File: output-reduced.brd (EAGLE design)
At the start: 31.8 x 81.7 mm, 84 parts

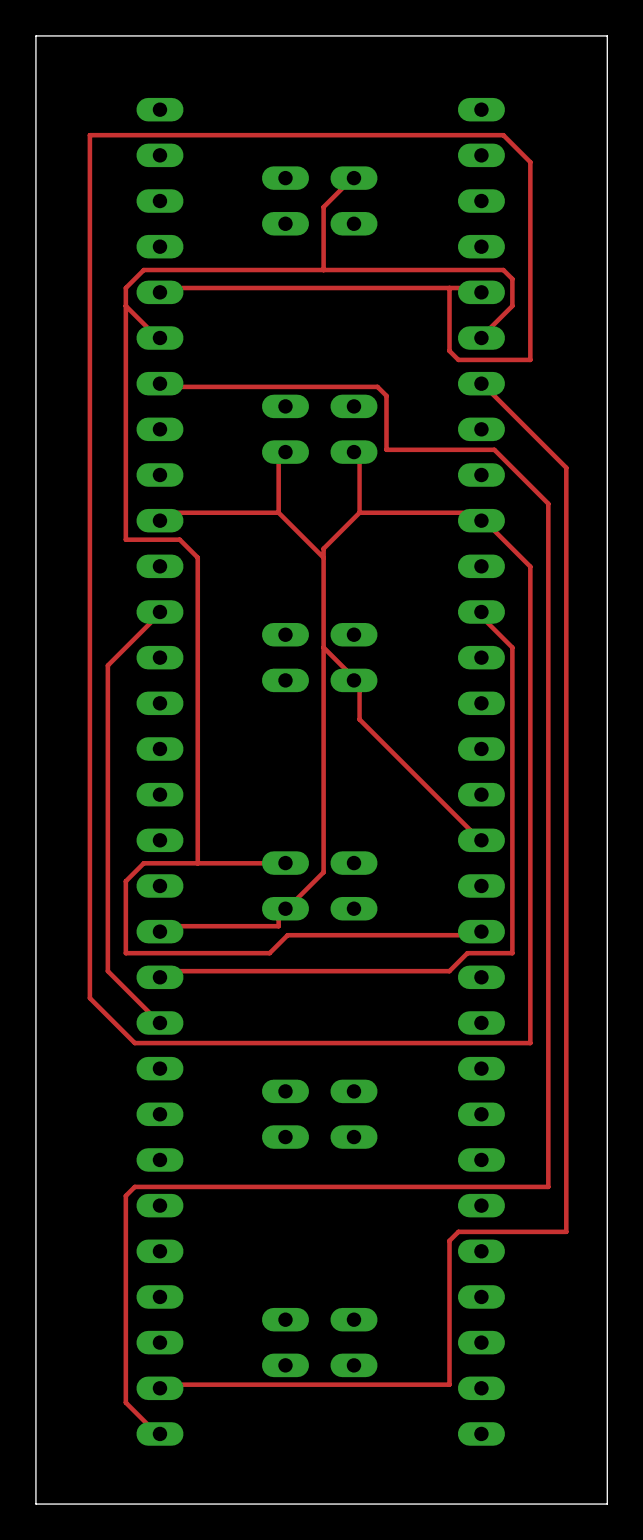
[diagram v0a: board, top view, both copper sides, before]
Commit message: new CirclingCar circuit
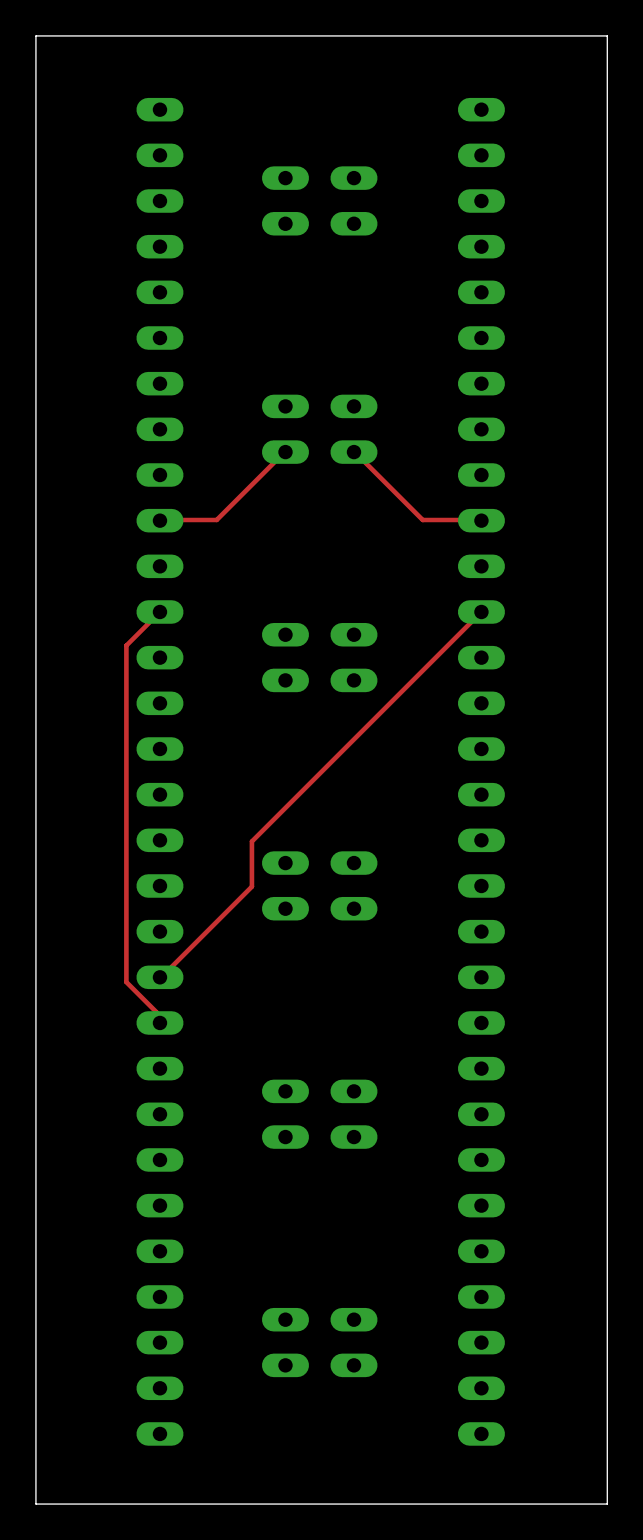
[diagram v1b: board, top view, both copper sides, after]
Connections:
- removed net SIGNAL4: LL5.P$1, LS6.P$1, RL18.P$1, RL5.P$1, RS0.P$1
- removed net SIGNAL5: LL18.P$1, LL4.P$1, LL9.P$1, LS3.P$1, LS7.P$1, RL16.P$1, RL4.P$1, RL9.P$1, RS3.P$1, RS5.P$1
- net SIGNAL0: now also LL19.P$1, RL11.P$1; no longer LL28.P$1, RL6.P$1
- net SIGNAL1: now also LL11.P$1, LL20.P$1; no longer LL29.P$1, LL6.P$1
- net SIGNAL2: now also LL9.P$1, LS3.P$1; no longer LL19.P$1, RL11.P$1
- net SIGNAL3: now also RL9.P$1, RS3.P$1; no longer LL11.P$1, LL20.P$1
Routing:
- net SIGNAL5: track 237.1 -> 0.00 mm
- net SIGNAL4: track 103.5 -> 0.00 mm
- net SIGNAL1: track 101.9 -> 24.5 mm
- net SIGNAL0: track 80.1 -> 27.8 mm
- net SIGNAL2: track 39.9 -> 8.54 mm
- net SIGNAL3: track 25.2 -> 8.65 mm
